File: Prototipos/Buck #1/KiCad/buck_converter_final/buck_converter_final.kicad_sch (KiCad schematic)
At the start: 48 parts, among them J2 Screw_Terminal_01x02, J3 Screw_Terminal_01x02, K1 SANYOU_SRD_Form_C, Q1 NPN, Q2 IRF9540NPBF, Q3 BC548, U1 INA199xxDCK, U2 INA199xxDCK, U4 TL071HIDBVR

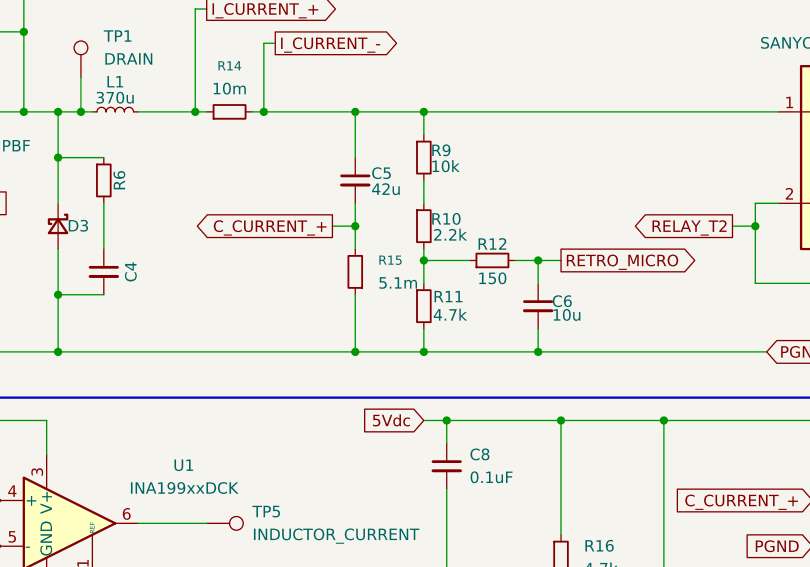
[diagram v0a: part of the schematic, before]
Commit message: Actualizar huella resistencia shunt
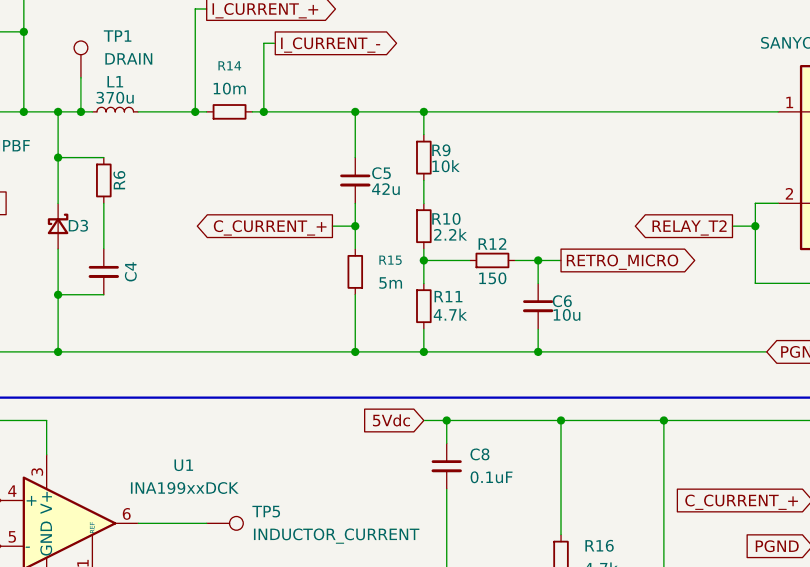
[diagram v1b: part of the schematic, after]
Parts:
- R14: footprint Resistor_SMD:R_0805_2012Metric_Pad1.20x1.40mm_HandSolder -> Resistor_SMD:R_2512_6332Metric_Pad1.40x3.35mm_HandSolder
- R15: value 5.1m -> 5m; footprint Resistor_SMD:R_0805_2012Metric_Pad1.20x1.40mm_HandSolder -> Resistor_SMD:R_2512_6332Metric_Pad1.40x3.35mm_HandSolder
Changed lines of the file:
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@@
 			)
 		)
-		(property "Value" "5.1m"
+		(property "Value" "5m"
 			(at 156.21 54.6099 0)
 			(effects
@@
 			)
 		)
-		(property "Footprint" "Resistor_SMD:R_0805_2012Metric_Pad1.20x1.40mm_HandSolder"
+		(property "Footprint" "Resistor_SMD:R_2512_6332Metric_Pad1.40x3.35mm_HandSolder"
 			(at 153.67 53.34 0)
 			(effects
@@
 			)
 		)
-		(property "Footprint" "Resistor_SMD:R_0805_2012Metric_Pad1.20x1.40mm_HandSolder"
+		(property "Footprint" "Resistor_SMD:R_2512_6332Metric_Pad1.40x3.35mm_HandSolder"
 			(at 139.7 35.56 0)
 			(effects

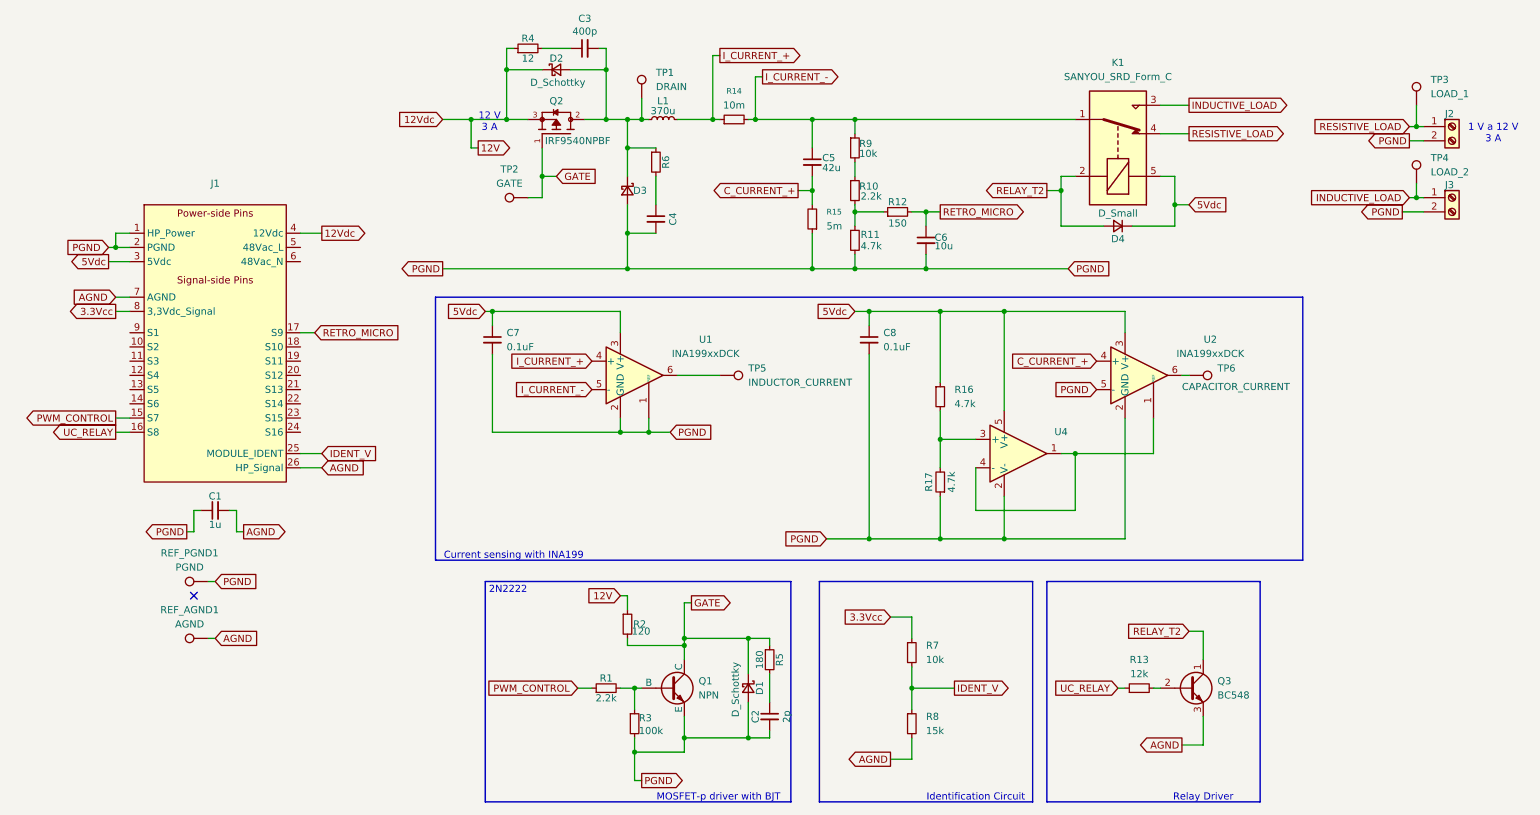
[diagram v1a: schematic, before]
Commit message: Comenzar rediseño placa Buck
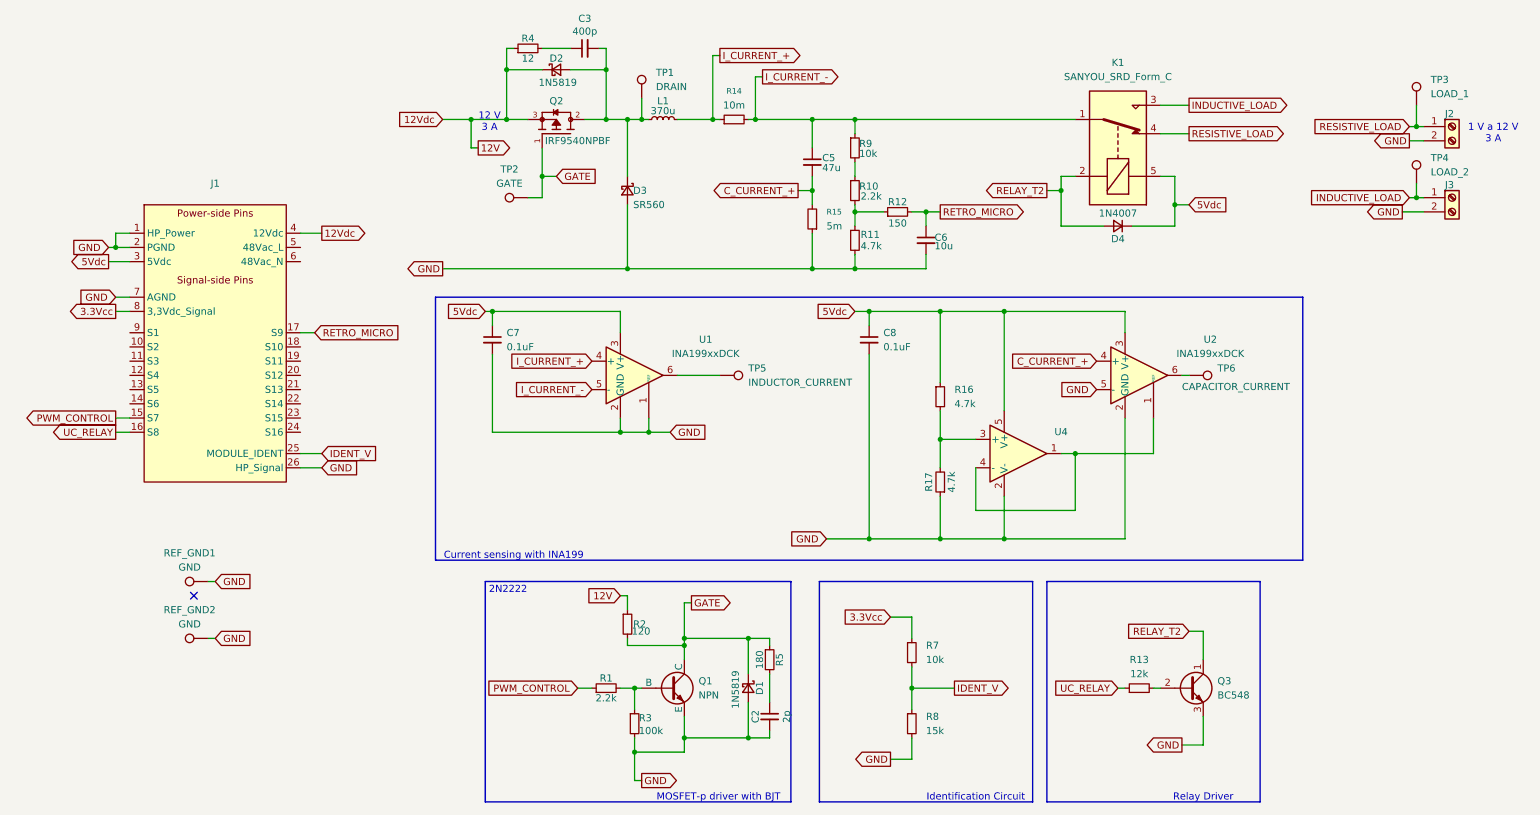
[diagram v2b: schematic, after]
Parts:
- removed C1: 1u, Capacitor_THT:C_Disc_D3.8mm_W2.6mm_P2.50mm, symbol Device:C_Small
- removed C4: ~, Capacitor_THT:C_Disc_D3.8mm_W2.6mm_P2.50mm, symbol Device:C_Small
- removed R6: ~, Resistor_THT:R_Axial_DIN0207_L6.3mm_D2.5mm_P7.62mm_Horizontal, symbol Device:R_Small
- C5: value 42u -> 47u; footprint Capacitor_THT:C_Disc_D3.8mm_W2.6mm_P2.50mm -> Capacitor_THT:C_Radial_D5.0mm_H11.0mm_P2.00mm
- C6: footprint Capacitor_THT:C_Disc_D3.8mm_W2.6mm_P2.50mm -> Capacitor_THT:C_Radial_D4.0mm_H7.0mm_P1.50mm
- D1, D2: value D_Schottky -> 1N5819
- D3: value D_Schottky -> SR560
- D4: value D_Small -> 1N4007
- REF_GND1: renamed from REF_PGND1; value PGND -> GND
- REF_GND2: renamed from REF_AGND1; value AGND -> GND
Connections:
- net PGND is gone; now on net GND: C2.2, C6.2, C7.2, C8.2, D1.2 (A), D3.2 (A), J1.1 (HP_Power), J1.2 (PGND), J2.2 (Pin_2), J3.2 (Pin_2), Q1.1 (E), R11.2, R15.1, R17.1, R3.2, REF_GND1.1, U1.1 (REF), U1.2 (GND), U2.2 (GND), U2.5 (-), U4.2 (V-)
- net AGND renamed GND
